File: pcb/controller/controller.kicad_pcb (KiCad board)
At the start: 2 copper layers, 90 x 65 mm, 41 parts, among them J1 Barrel_Jack, J2 AVR-ISP-6, U1 ATmega328P-A, Y1 Crystal_GND24

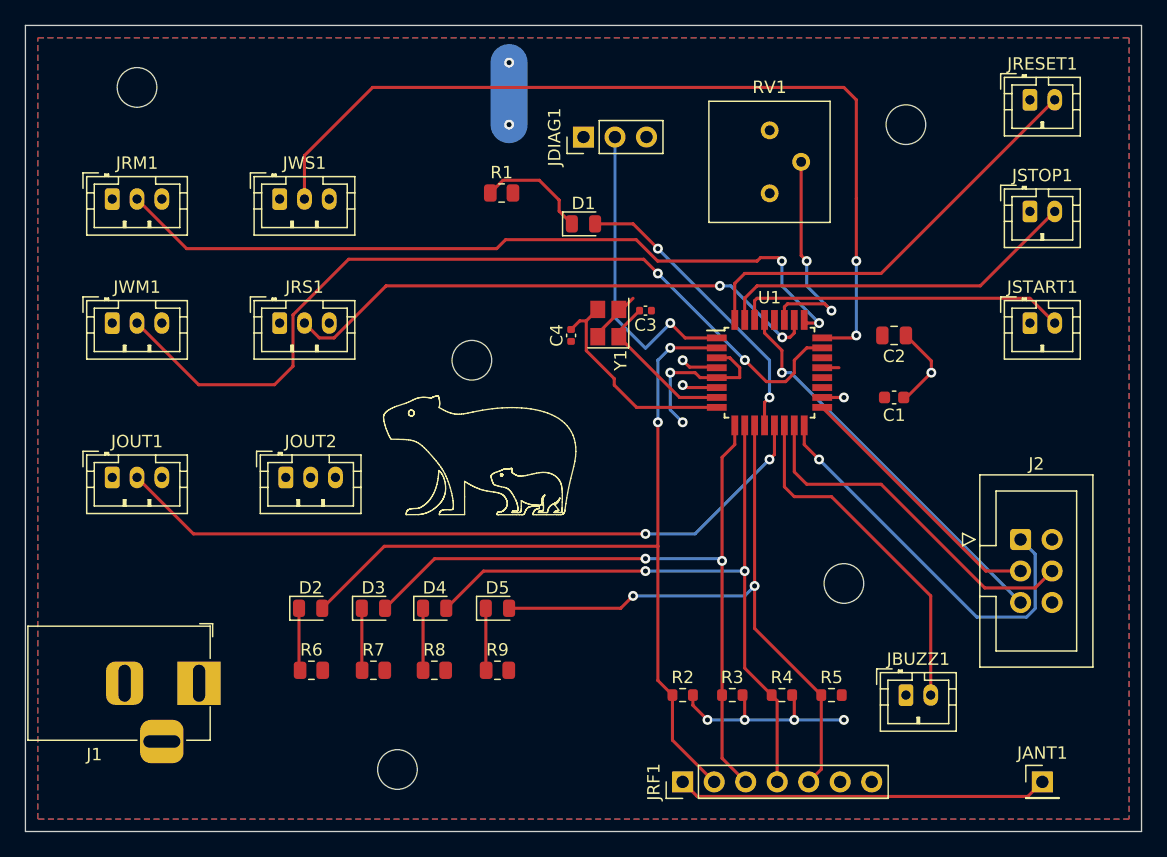
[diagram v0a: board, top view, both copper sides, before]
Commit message: Added Volume Control
This adds a volume control potentiometer to the schematic and PCB
design for the control board
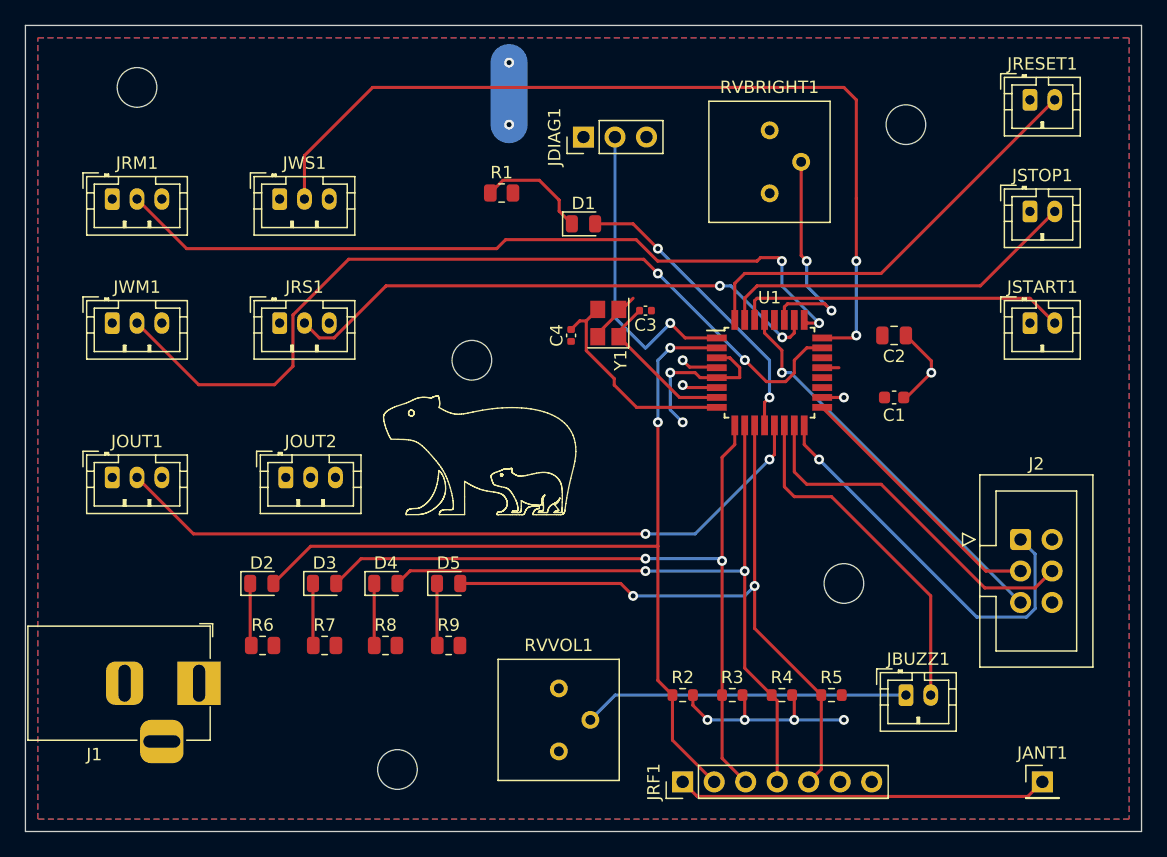
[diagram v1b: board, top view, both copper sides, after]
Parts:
- added RVVOL1: R_Potentiometer, Potentiometer_THT:Potentiometer_Bourns_3386P_Vertical, F.Cu at (151.0, 122.5)
- moved D2 4.42 mm to (127.1, 109.0)
- moved D3 4.42 mm to (132.1, 109.0)
- moved D4 4.42 mm to (137.1, 109.0)
- moved D5 4.42 mm to (142.1, 109.0)
- moved R6 4.42 mm to (127.1, 114.0)
- moved R7 4.42 mm to (132.1, 114.0)
- moved R8 4.42 mm to (137.0, 114.0)
- moved R9 4.42 mm to (142.1, 114.0)
- renumbered RV1 to RVBRIGHT1
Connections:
- JBUZZ1 pad 1: GND -> Net-(JBUZZ1-Pad1)
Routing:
- net Net-(JBUZZ1-Pad1): track 0.00 -> 26.3 mm
- net Net-(D5-Pad2): track 51.9 -> 55.9 mm
- net Net-(D4-Pad2): track 55.1 -> 58.3 mm
- net Net-(D3-Pad2): track 58.9 -> 62.0 mm
- net Net-(D2-Pad2): track 70.2 -> 73.3 mm

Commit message: Added MOSFET to Controller Board for Buzzer
I want to allow the use of some higher powered piezo buzzers, so this
adds a MOSFET to switch the buzzer current instead of connecting it
directly to the Atmega pin.
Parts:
- added Q1: 2N7002, Package_TO_SOT_SMD:SOT-23, F.Cu at (180.0, 112.0)
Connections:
- JBUZZ1 pad 2: Net-(JBUZZ1-Pad2) -> +5V
- RVVOL1 pad 2: Net-(JBUZZ1-Pad1) -> Net-(RVVOL1-Pad2)
- U1 pad 14: Net-(JBUZZ1-Pad2) -> Net-(U1-Pad14)
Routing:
- net Net-(RVVOL1-Pad2): track 0.00 -> 30.8 mm, vias 0 -> 1
- net Net-(JBUZZ1-Pad2): track 28.4 -> 0.00 mm
- net Net-(U1-Pad14): track 0.00 -> 20.6 mm
- net Net-(JBUZZ1-Pad1): track 26.3 -> 6.80 mm

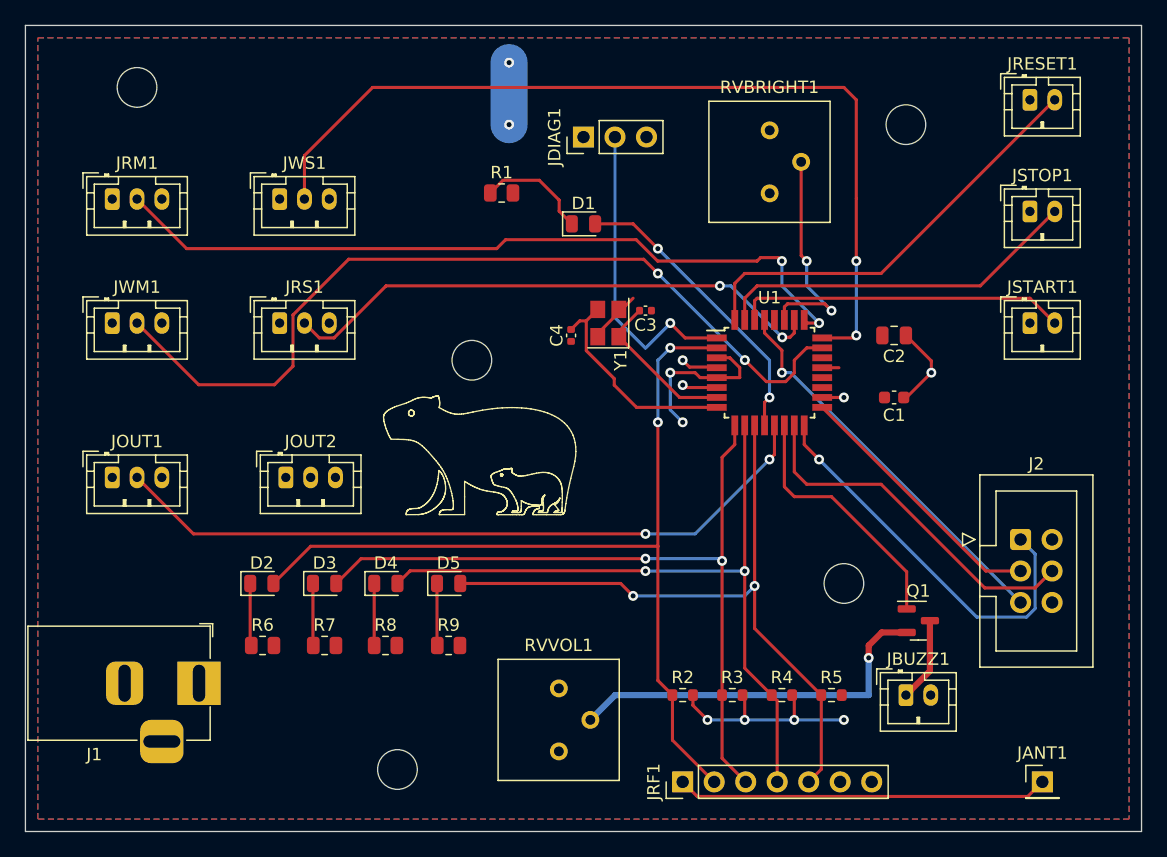
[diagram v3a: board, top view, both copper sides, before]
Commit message: PCB Touchup
Two changes in this commit.

1. I rewired the volume potentiometer so that the MOSFET is now the
closest thing to ground.  That way we'll always be sure to have
sufficient gate-source voltage to trigger it when the buzzer is turned
on.

2. I added v1/date indicators to the silk screen layers of all the
PCBs.
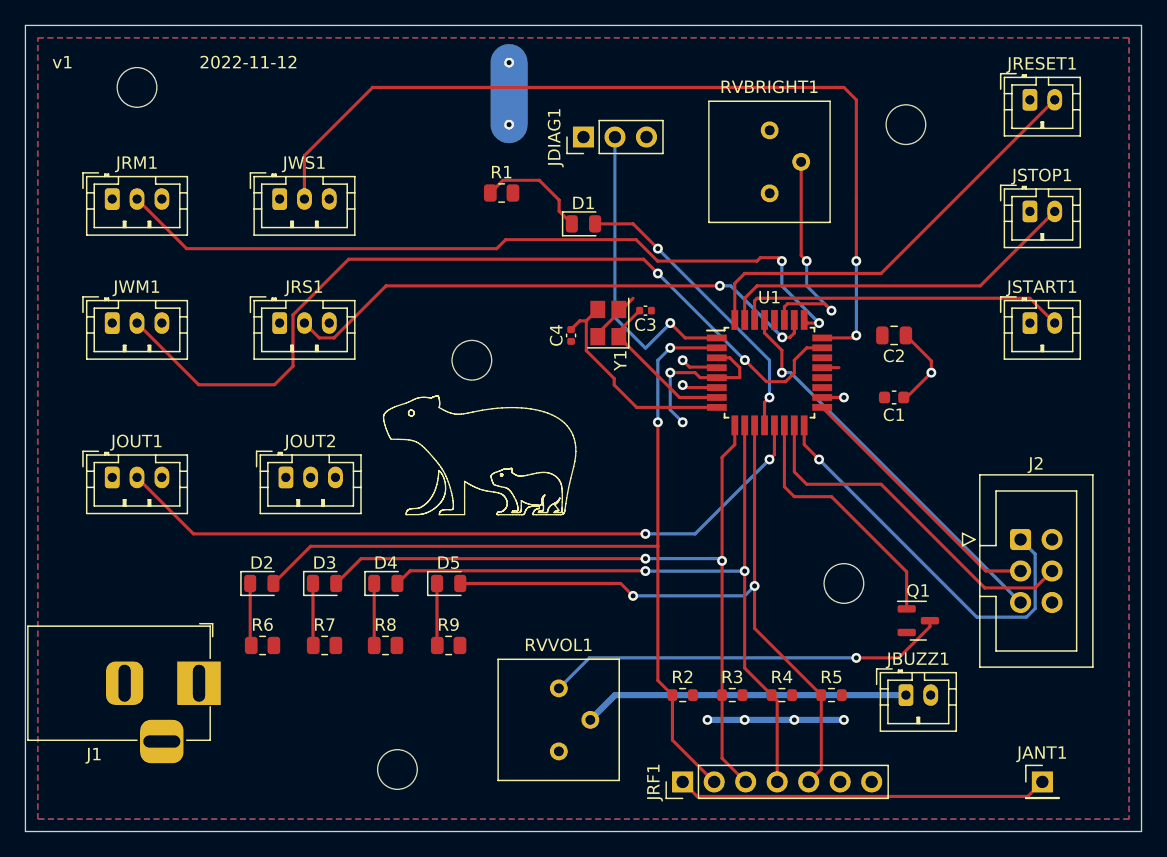
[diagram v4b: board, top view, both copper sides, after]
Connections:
- Q1 pad 2: Net-(RVVOL1-Pad2) -> GND
- Q1 pad 3: Net-(JBUZZ1-Pad1) -> Net-(Q1-Pad3)
- RVVOL1 pad 2: Net-(RVVOL1-Pad2) -> Net-(JBUZZ1-Pad1)
- RVVOL1 pad 3: GND -> Net-(Q1-Pad3)
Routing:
- net Net-(Q1-Pad3): track 0.00 -> 32.5 mm, vias 0 -> 1
- net Net-(RVVOL1-Pad2): track 30.8 -> 0.00 mm, vias 1 -> 0
- net Net-(JBUZZ1-Pad1): track 6.80 -> 26.3 mm
- net GND: track 41.6 -> 35.4 mm
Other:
- board text added: "2022-11-12"
- board text added: "v1"
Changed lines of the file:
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@@
   (net 35 "Net-(RVBRIGHT1-Pad2)")
   (net 36 "unconnected-(RVVOL1-Pad1)")
-  (net 37 "Net-(U1-Pad14)")
-  (net 38 "Net-(RVVOL1-Pad2)")
+  (net 37 "Net-(Q1-Pad1)")
+  (net 38 "Net-(Q1-Pad3)")
   (footprint "Capacitor_SMD:C_0402_1005Metric" (layer "F.Cu")
     (at 152 89 90)
@@
       (net 20 "Net-(JOUT1-Pad2)") (pinfunction "PB1") (pintype "bidirectional"))
     (pad "14" smd rect (at 1.2 4.25 90) (size 1.6 0.55) (layers "F.Cu" "F.Paste" "F.Mask")
-      (net 37 "Net-(U1-Pad14)") (pinfunction "PB2") (pintype "bidirectional"))
+      (net 37 "Net-(Q1-Pad1)") (pinfunction "PB2") (pintype "bidirectional"))
     (pad "15" smd rect (at 2 4.25 90) (size 1.6 0.55) (layers "F.Cu" "F.Paste" "F.Mask")
       (net 17 "Net-(J2-Pad4)") (pinfunction "PB3") (pintype "bidirectional"))
@@
       (net 36 "unconnected-(RVVOL1-Pad1)") (pinfunction "1") (pintype "passive+no_connect"))
     (pad "2" thru_hole circle (at 2.54 -2.54) (size 1.44 1.44) (drill 0.8) (layers *.Cu *.Mask)
-      (net 38 "Net-(RVVOL1-Pad2)") (pinfunction "2") (pintype "passive"))
+      (net 29 "Net-(JBUZZ1-Pad1)") (pinfunction "2") (pintype "passive"))
     (pad "3" thru_hole circle (at 0 -5.08) (size 1.44 1.44) (drill 0.8) (layers *.Cu *.Mask)
-      (net 2 "GND") (pinfunction "3") (pintype "passive"))
+      (net 38 "Net-(Q1-Pad3)") (pinfunction "3") (pintype "passive"))
     (model "${KICAD6_3DMODEL_DIR}/Potentiometer_THT.3dshapes/Potentiometer_Bourns_3386P_Vertical.wrl"
       (offset (xyz 0 0 0))
@@
     (fp_line (start -0.325 -1.45) (end 0.65 -1.45) (layer "F.Fab") (width 0.1))
     (pad "1" smd roundrect (at -0.9375 -0.95) (size 1.475 0.6) (layers "F.Cu" "F.Paste" "F.Mask") (roundrect_rratio 0.25)
-      (net 37 "Net-(U1-Pad14)") (pinfunction "G") (pintype "input"))
+      (net 37 "Net-(Q1-Pad1)") (pinfunction "G") (pintype "input"))
     (pad "2" smd roundrect (at -0.9375 0.95) (size 1.475 0.6) (layers "F.Cu" "F.Paste" "F.Mask") (roundrect_rratio 0.25)
-      (net 38 "Net-(RVVOL1-Pad2)") (pinfunction "S") (pintype "passive"))
+      (net 2 "GND") (pinfunction "S") (pintype "passive"))
     (pad "3" smd roundrect (at 0.9375 0) (size 1.475 0.6) (layers "F.Cu" "F.Paste" "F.Mask") (roundrect_rratio 0.25)
-      (net 29 "Net-(JBUZZ1-Pad1)") (pinfunction "D") (pintype "passive"))
+      (net 38 "Net-(Q1-Pad3)") (pinfunction "D") (pintype "passive"))
     (model "${KICAD6_3DMODEL_DIR}/Package_TO_SOT_SMD.3dshapes/SOT-23.wrl"
       (offset (xyz 0 0 0))
@@
   (gr_line (start 148.31314 103.174969) (end 148.330331 103.135244) (layer "F.SilkS") (width 0.06))
   (gr_rect (start 198 64) (end 108 129) (layer "Edge.Cuts") (width 0.1) (fill none))
+  (gr_text "2022-11-12" (at 126 67) (layer "F.SilkS")
+    (effects (font (size 1 1) (thickness 0.15)))
+  )
+  (gr_text "v1" (at 111 67) (layer "F.SilkS")
+    (effects (font (size 1 1) (thickness 0.15)))
+  )
   (segment (start 181.05 91.05) (end 179 89) (width 0.25) (layer "F.Cu") (net 1))
   (segment (start 161.55048 91.55048) (end 161 91) (width 0.25) (layer "F.Cu") (net 1))
@@
   (via (at 161 91) (size 0.8) (drill 0.4) (layers "F.Cu" "B.Cu") (net 1))
   (via (at 161 93) (size 0.8) (drill 0.4) (layers "F.Cu" "B.Cu") (net 1))
-  (segment (start 161.825 118) (end 161.825 118.825) (width 0.25) (layer "F.Cu") (net 2))
   (segment (start 155.85 86.9) (end 156.1 86.9) (width 0.25) (layer "F.Cu") (net 2))
   (segment (start 156.1 86.9) (end 157 86) (width 0.25) (layer "F.Cu") (net 2))
@@
   (segment (start 155.85 86.9) (end 155.85 87.15) (width 0.25) (layer "F.Cu") (net 2))
   (segment (start 170 118.175) (end 169.825 118) (width 0.25) (layer "F.Cu") (net 2))
-  (segment (start 166 120) (end 166 118.175) (width 0.25) (layer "F.Cu") (net 2))
   (segment (start 154.15 88.85) (end 154.15 89.1) (width 0.25) (layer "F.Cu") (net 2))
   (segment (start 166 118.175) (end 165.825 118) (width 0.25) (layer "F.Cu") (net 2))
@@
   (segment (start 172.25 91.6) (end 173.6 91.6) (width 0.25) (layer "F.Cu") (net 2))
   (segment (start 162.4 92.4) (end 162 92) (width 0.25) (layer "F.Cu") (net 2))
-  (segment (start 161.825 118.825) (end 163 120) (width 0.25) (layer "F.Cu") (net 2))
   (segment (start 164.8 90.8) (end 165.6 91.6) (width 0.25) (layer "F.Cu") (net 2))
-  (segment (start 170 120) (end 170 118.175) (width 0.25) (layer "F.Cu") (net 2))
   (via (at 174 120) (size 0.8) (drill 0.4) (layers "F.Cu" "B.Cu") (net 2))
   (via (at 161 96) (size 0.8) (drill 0.4) (layers "F.Cu" "B.Cu") (net 2))
@@
   (via (at 163 120) (size 0.8) (drill 0.4) (layers "F.Cu" "B.Cu") (net 2))
   (via (at 160 92) (size 0.8) (drill 0.4) (layers "F.Cu" "B.Cu") (net 2))
-  (segment (start 163 120) (end 166 120) (width 0.25) (layer "B.Cu") (net 2))
   (segment (start 160 95) (end 161 96) (width 0.25) (layer "B.Cu") (net 2))
   (segment (start 160 92) (end 160 95) (width 0.25) (layer "B.Cu") (net 2))
-  (segment (start 166 120) (end 170 120) (width 0.25) (layer "B.Cu") (net 2))
-  (segment (start 170 120) (end 174 120) (width 0.25) (layer "B.Cu") (net 2))
+  (segment (start 166 120) (end 163 120) (width 0.5) (layer "B.Cu") (net 2))
+  (segment (start 166 120) (end 170 120) (width 0.5) (layer "B.Cu") (net 2))
+  (segment (start 170 120) (end 174 120) (width 0.5) (layer "B.Cu") (net 2))
   (segment (start 147 72) (end 147 67) (width 3) (layer "B.Cu") (net 2))
   (segment (start 155.85 88.67) (end 155.85 89.1) (width 0.25) (layer "F.Cu") (net 3))
@@
   (via (at 175 83) (size 0.8) (drill 0.4) (layers "F.Cu" "B.Cu") (net 28))
   (segment (start 175 83) (end 175 89) (width 0.25) (layer "B.Cu") (net 28))
-  (segment (start 180.9375 116.0625) (end 179 118) (width 0.5) (layer "F.Cu") (net 29))
-  (segment (start 180.9375 112) (end 180.9375 116.0625) (width 0.5) (layer "F.Cu") (net 29))
+  (segment (start 155.555 118) (end 179 118) (width 0.5) (layer "B.Cu") (net 29))
+  (segment (start 153.555 120) (end 155.555 118) (width 0.5) (layer "B.Cu") (net 29))
   (segment (start 163.75 89.2) (end 161.2 89.2) (width 0.25) (layer "F.Cu") (net 30))
   (segment (start 161.2 89.2) (end 160 88) (width 0.25) (layer "F.Cu") (net 30))
@@
   (segment (start 179.0625 108.0625) (end 179.0625 111.05) (width 0.25) (layer "F.Cu") (net 37))
   (segment (start 170 102) (end 173 102) (width 0.25) (layer "F.Cu") (net 37))
-  (segment (start 176 115) (end 176 114) (width 0.5) (layer "F.Cu") (net 38))
-  (segment (start 177.05 112.95) (end 179.0625 112.95) (width 0.5) (layer "F.Cu") (net 38))
-  (segment (start 176 114) (end 177.05 112.95) (width 0.5) (layer "F.Cu") (net 38))
-  (via (at 176 115) (size 0.8) (drill 0.4) (layers "F.Cu" "B.Cu") (net 38))
-  (segment (start 176 118) (end 176 115) (width 0.5) (layer "B.Cu") (net 38))
-  (segment (start 155.555 118) (end 176 118) (width 0.5) (layer "B.Cu") (net 38))
-  (segment (start 153.555 120) (end 155.555 118) (width 0.5) (layer "B.Cu") (net 38))
+  (segment (start 178.421072 115) (end 175 115) (width 0.25) (layer "F.Cu") (net 38))
+  (segment (start 180.9375 112.483572) (end 178.421072 115) (width 0.25) (layer "F.Cu") (net 38))
+  (segment (start 180.9375 112) (end 180.9375 112.483572) (width 0.25) (layer "F.Cu") (net 38))
+  (via (at 175 115) (size 0.8) (drill 0.4) (layers "F.Cu" "B.Cu") (net 38))
+  (segment (start 175 115) (end 153.475 115) (width 0.25) (layer "B.Cu") (net 38))
+  (segment (start 153.475 115) (end 151.015 117.46) (width 0.25) (layer "B.Cu") (net 38))
   (zone (net 2) (net_name "GND") (layer "F.Cu") (hatch edge 0.508)
     (connect_pads (clearance 0.508))

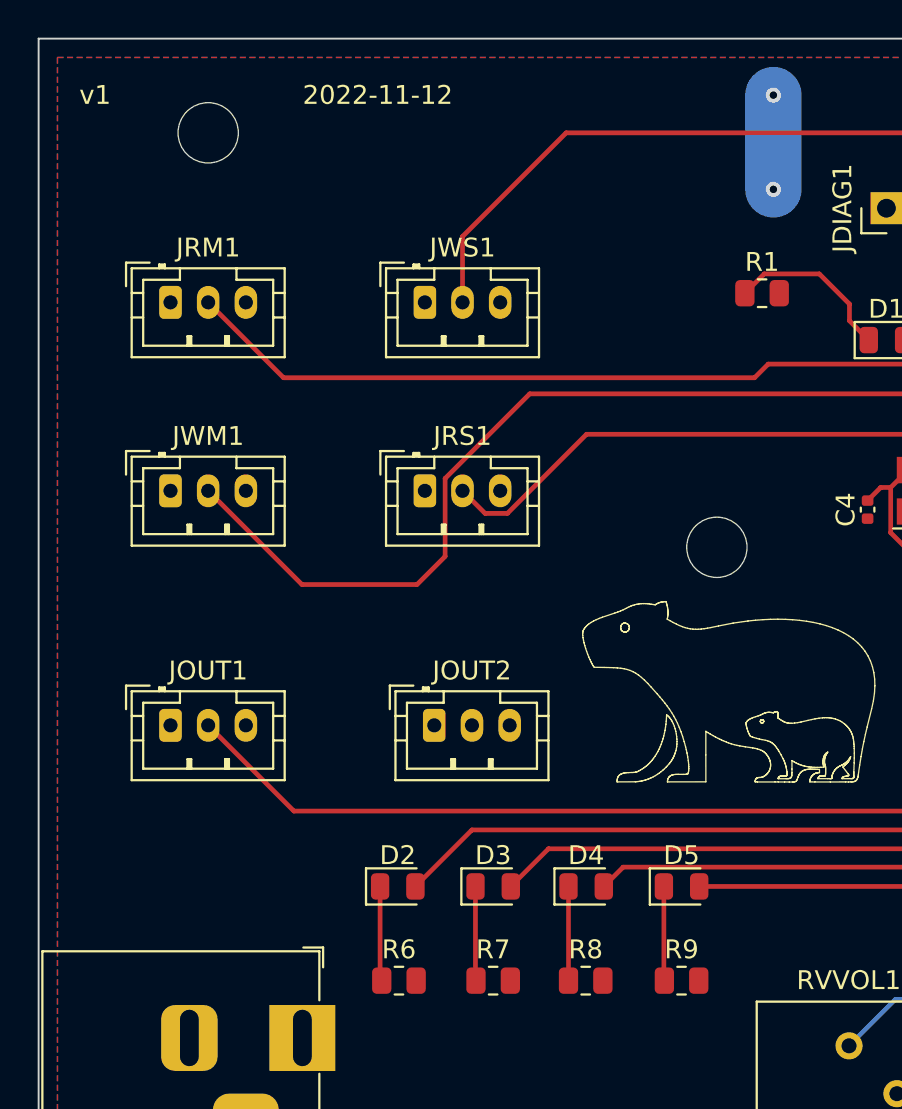
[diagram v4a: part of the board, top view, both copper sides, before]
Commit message: Bump Up LED Resistors
The LEDs on the controller board are very bright in the first batch of
boards, so this replaces the 470ohm resistors with 1k resistors to dim
them a little.
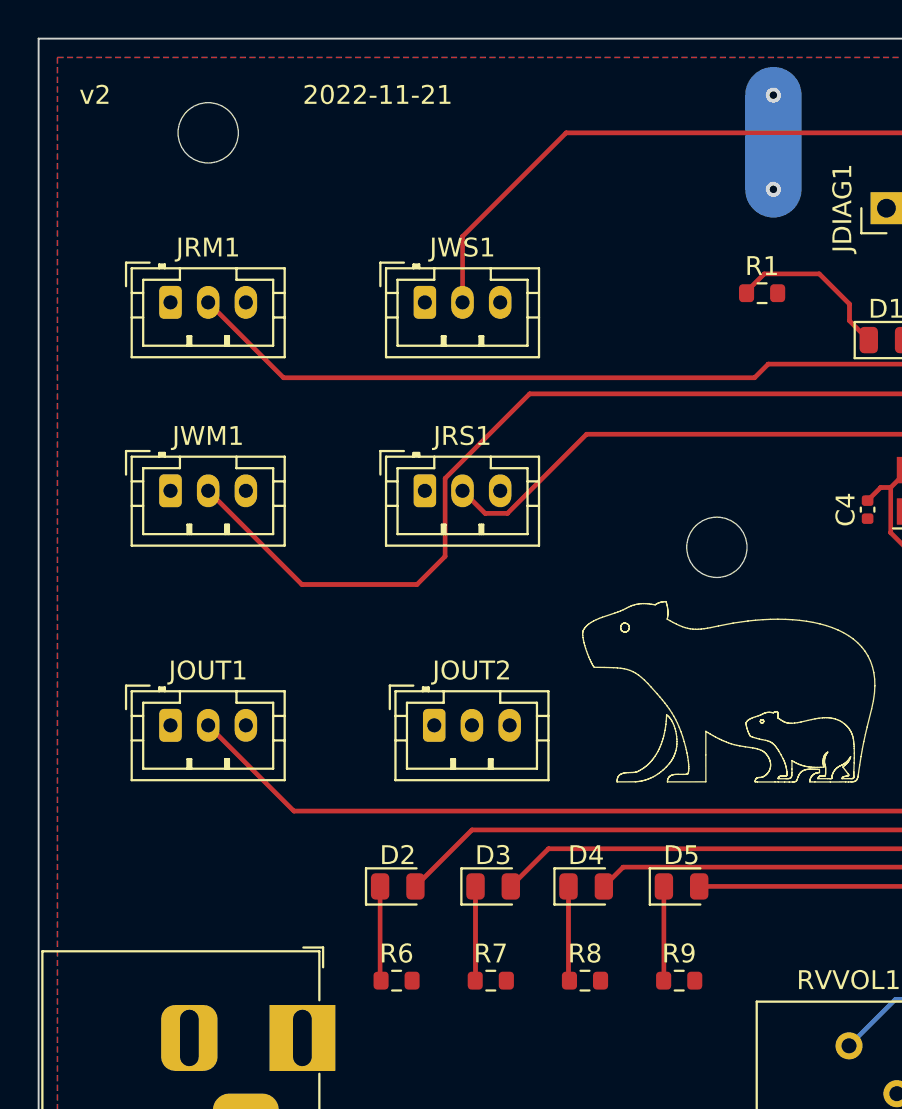
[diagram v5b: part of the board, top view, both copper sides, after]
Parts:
- R1, R6, R7, R8, R9: value 470Ω -> 1kΩ; footprint Resistor_SMD:R_0805_2012Metric -> Resistor_SMD:R_0603_1608Metric
- moved R6 0.12 mm to (127.0, 114.0)
- moved R7 0.12 mm to (132.0, 114.0)
- moved R9 0.12 mm to (142.0, 114.0)
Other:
- board text added: "2022-11-21"
- board text added: "v2"
- board text removed: "2022-11-12"
- board text removed: "v1"
